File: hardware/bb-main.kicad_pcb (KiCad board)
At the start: 2 copper layers, 1 part, among them U2 BU33TD3WG-TR

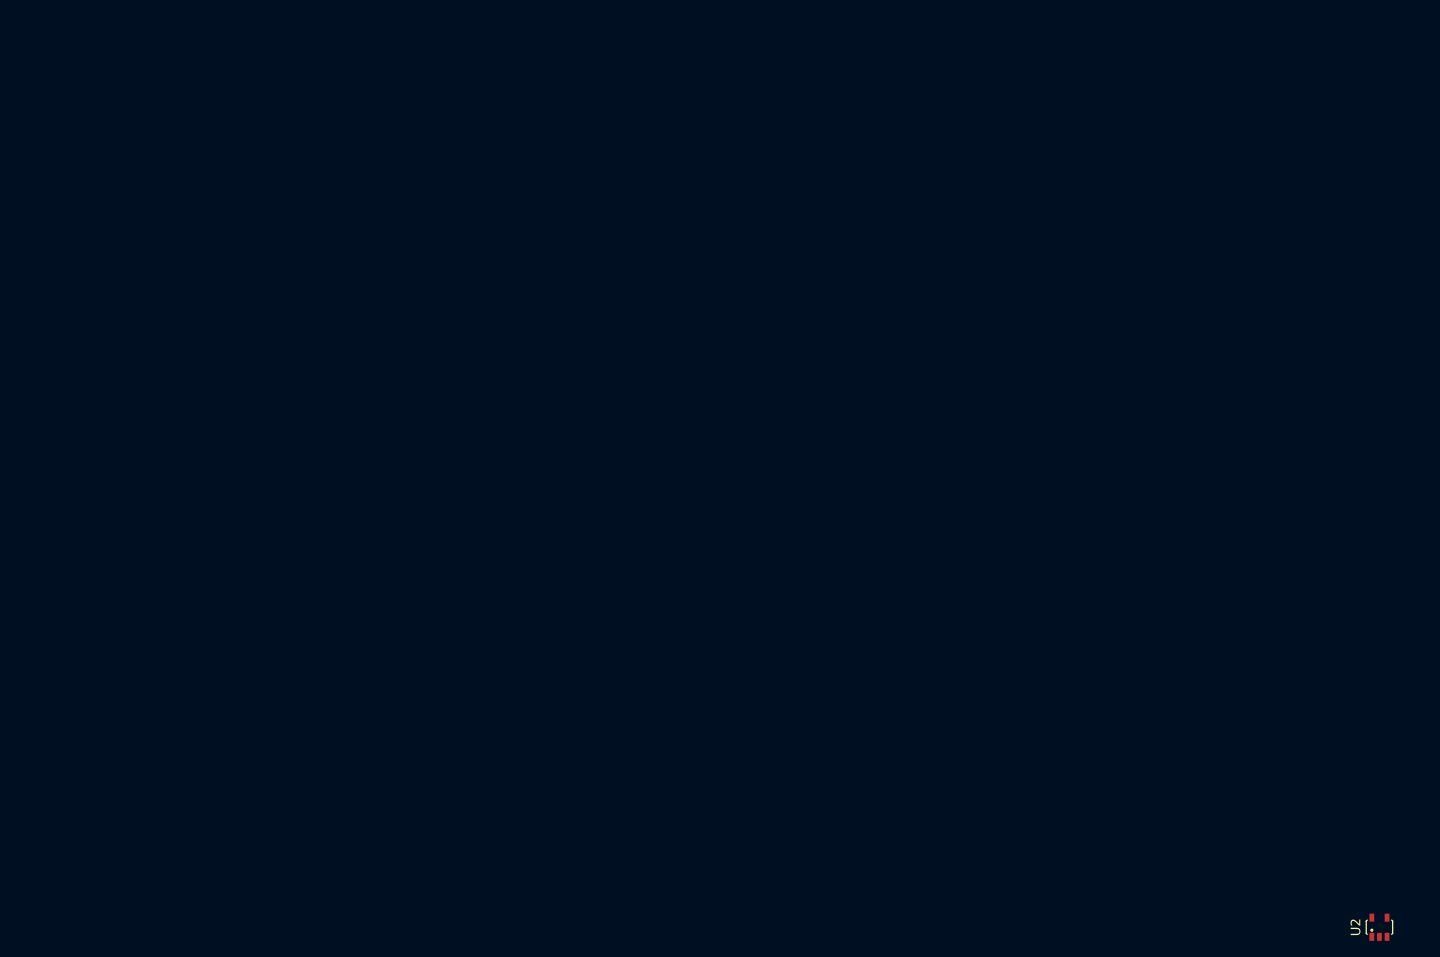
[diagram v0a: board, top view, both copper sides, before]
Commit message: Draw schematic components
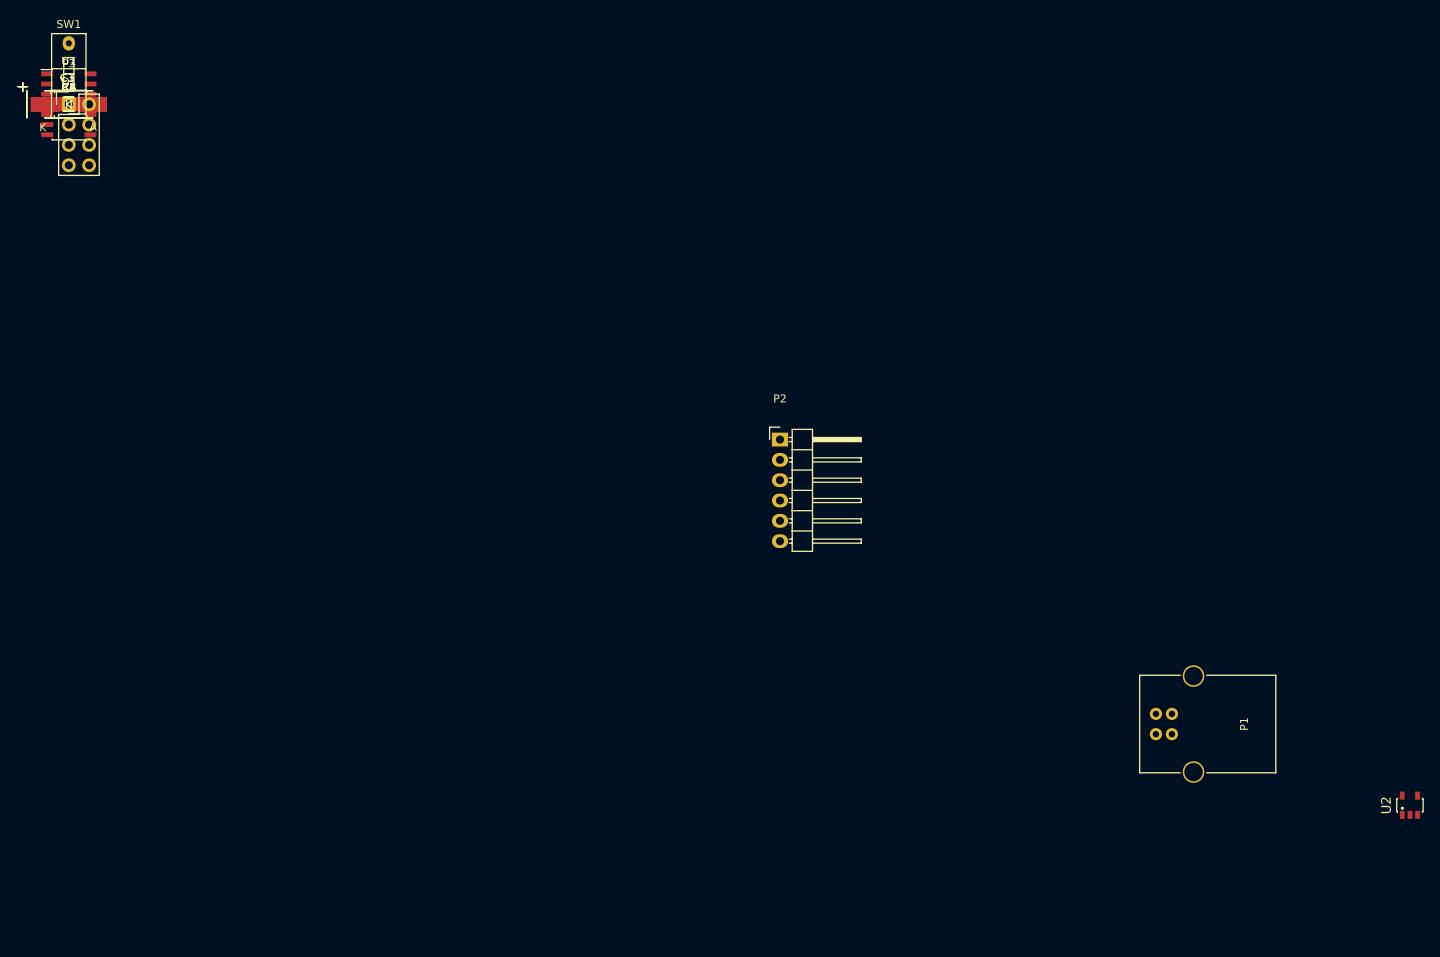
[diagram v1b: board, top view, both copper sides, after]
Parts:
- added C1: 10nF, Capacitors_Tantalum_SMD:TantalC_SizeC_EIA-6032_HandSoldering, F.Cu at (0.00, 0.00)
- added C2, C4: 100nF, Capacitors_SMD:C_0805_HandSoldering, F.Cu at (0.00, 0.00)
- added C3: 4.7uF, Capacitors_Tantalum_SMD:TantalC_SizeC_EIA-6032_HandSoldering, F.Cu at (0.00, 0.00)
- added C5, C6, C7: C, Capacitors_SMD:C_0805_HandSoldering, F.Cu at (0.00, 0.00)
- added D1: Led_Small, Diodes_SMD:SMA_Handsoldering, F.Cu at (0.00, 0.00)
- added P1: USB_B, Connect:USB_B, F.Cu at (135.9, 76.2)
- added P2: PICkit3, Pin_Headers:Pin_Header_Angled_1x06, F.Cu at (88.9, 41.9)
- added P3: OLED, Pin_Headers:Pin_Header_Straight_2x04, F.Cu at (0.00, 0.00)
- added R1: 10k, Resistors_SMD:R_0805_HandSoldering, F.Cu at (0.00, 0.00)
- added R2, R3, R4, R5: 4.7k, Resistors_SMD:R_0805_HandSoldering, F.Cu at (0.00, 0.00)
- added R6: 130, Resistors_SMD:R_0805_HandSoldering, F.Cu at (0.00, 0.00)
- added SW1: SW_PUSH, Buttons_Switches_ThroughHole:SW_DIP_x1_Slide, F.Cu at (0.00, 0.00)
- added U1: PIC16(L)F1455-I/SL, Housings_SOIC:SOIC-14_3.9x8.7mm_Pitch1.27mm, F.Cu at (0.00, 0.00)
- moved U2 15.7 mm to (167.6, 87.6)
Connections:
- U2 pad 1: Net-(U2-Pad1) -> +5V
- U2 pad 2: Net-(U2-Pad2) -> GND
- U2 pad 3: Net-(U2-Pad3) -> +5V
- U2 pad 5: Net-(U2-Pad5) -> +3V3

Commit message: Place components on the board
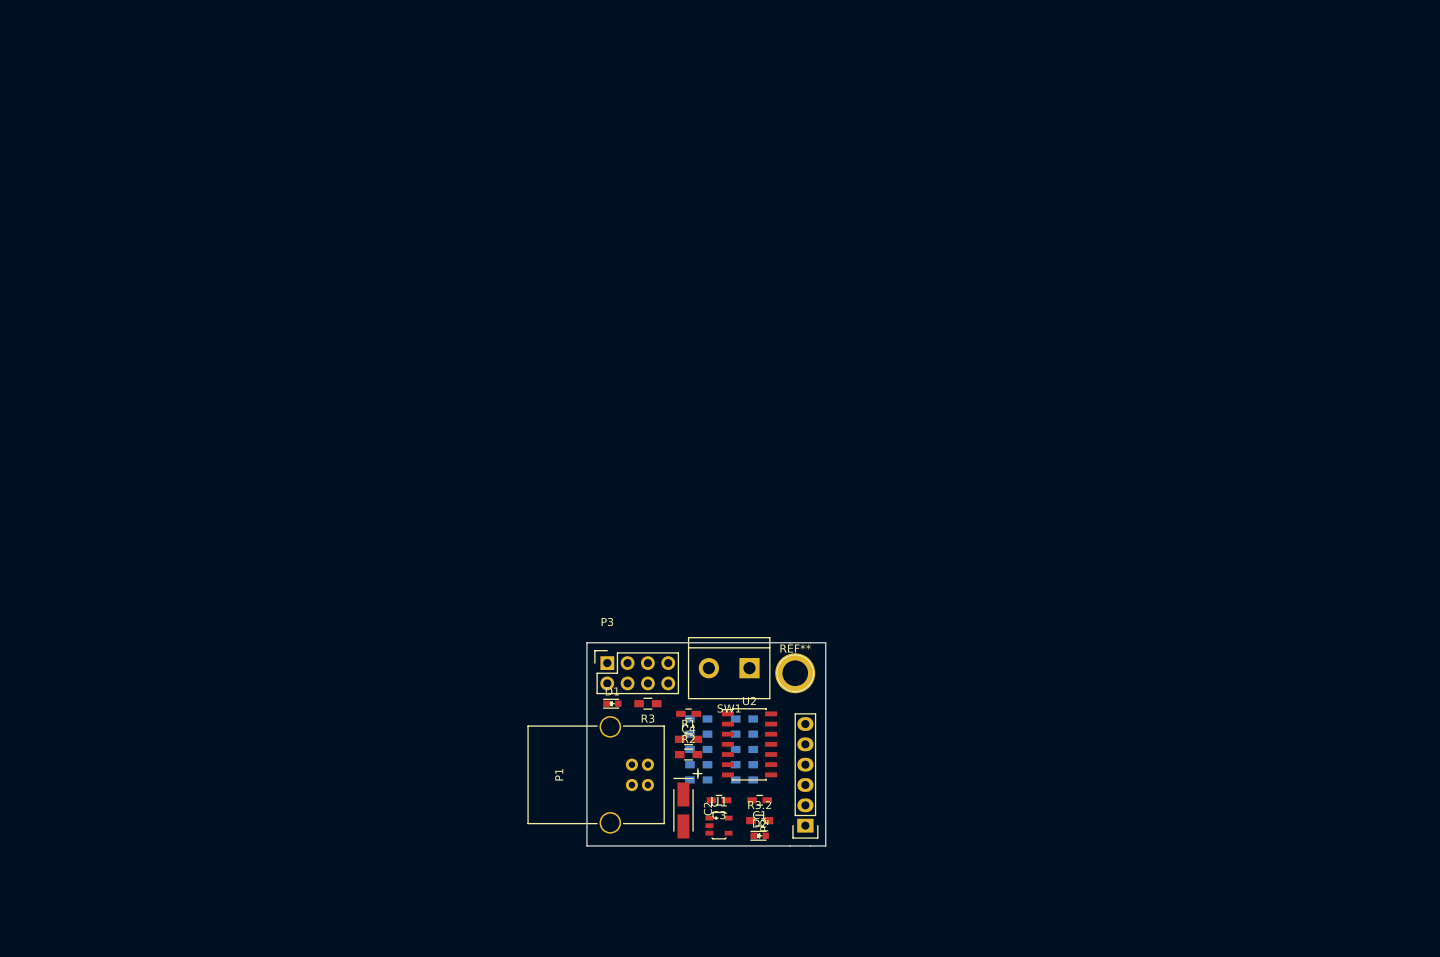
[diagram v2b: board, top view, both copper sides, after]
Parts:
- removed C5, C6, C7: C, Capacitors_SMD:C_0805_HandSoldering
- added D2: Led_Small, LEDs:LED_0603, F.Cu at (86.4, 91.4)
- added R10: 16k, Resistors_SMD:R_0603_HandSoldering, B.Cu at (78.7, 80.6)
- added R11: 16k, Resistors_SMD:R_0603_HandSoldering, B.Cu at (78.7, 82.5)
- added R12: 16k, Resistors_SMD:R_0603_HandSoldering, B.Cu at (78.7, 84.5)
- added R13: 16k, Resistors_SMD:R_0603_HandSoldering, B.Cu at (78.7, 76.8)
- added R3.2: 390, Resistors_SMD:R_0603_HandSoldering, F.Cu at (86.4, 89.5)
- added R7: 8.2k, Resistors_SMD:R_0603_HandSoldering, B.Cu at (84.5, 80.6)
- added R8: 8.2k, Resistors_SMD:R_0603_HandSoldering, B.Cu at (84.5, 78.7)
- added R9: 16k, Resistors_SMD:R_0603_HandSoldering, B.Cu at (78.7, 78.7)
- added REF**: 1pin, Connect:1pin, F.Cu at (90.8, 71.1)
- C1: value 10nF -> 470nF; footprint Capacitors_Tantalum_SMD:TantalC_SizeC_EIA-6032_HandSoldering -> Capacitors_SMD:C_0603_HandSoldering
- C2: value 100nF -> 10uF; footprint Capacitors_SMD:C_0805_HandSoldering -> Capacitors_Tantalum_SMD:TantalC_SizeA_EIA-3216_HandSoldering
- C3: value 4.7uF -> 100nF; footprint Capacitors_Tantalum_SMD:TantalC_SizeC_EIA-6032_HandSoldering -> Capacitors_SMD:C_0603_HandSoldering
- C4: footprint Capacitors_SMD:C_0805_HandSoldering -> Capacitors_SMD:C_0603_HandSoldering
- D1: footprint Diodes_SMD:SMA_Handsoldering -> LEDs:LED_0603
- P2: footprint Pin_Headers:Pin_Header_Angled_1x06 -> Socket_Strips:Socket_Strip_Straight_1x06
- P3: footprint Pin_Headers:Pin_Header_Straight_2x04 -> Socket_Strips:Socket_Strip_Straight_2x04
- R1: footprint Resistors_SMD:R_0805_HandSoldering -> Resistors_SMD:R_0603_HandSoldering
- R2: value 4.7k -> 10k; footprint Resistors_SMD:R_0805_HandSoldering -> Resistors_SMD:R_0603_HandSoldering
- R3: value 4.7k -> 390; footprint Resistors_SMD:R_0805_HandSoldering -> Resistors_SMD:R_0603_HandSoldering
- R4, R5: value 4.7k -> 8.2k; footprint Resistors_SMD:R_0805_HandSoldering -> Resistors_SMD:R_0603_HandSoldering; moved to B.Cu
- R6: value 130 -> 8.2k; footprint Resistors_SMD:R_0805_HandSoldering -> Resistors_SMD:R_0603_HandSoldering; moved to B.Cu
- SW1: footprint Buttons_Switches_ThroughHole:SW_DIP_x1_Slide -> Connect:bornier2
- U1: value PIC16(L)F1455-I/SL -> BU33TD3WG-TR; footprint Housings_SOIC:SOIC-14_3.9x8.7mm_Pitch1.27mm -> Housings_Proj:SSOP5
- U2: value BU33TD3WG-TR -> PIC16(L)F1455-I/SL; footprint SSOP5 -> Housings_SOIC:SOIC-14_3.9x8.7mm_Pitch1.27mm
- moved C1 122.6 mm to (86.4, 87.0), turned to 180 degrees
- moved U1 121.4 mm to (81.3, 90.2), turned to 270 degrees
- moved R5 119.4 mm to (84.5, 84.5), turned to 180 degrees
- moved C3 119.1 mm to (81.3, 87.0), turned to 180 degrees
- moved R6 118.1 mm to (84.5, 82.5), turned to 180 degrees
- moved C2 117.0 mm to (76.8, 88.3), turned to 270 degrees
- moved R4 114.2 mm to (84.5, 76.8), turned to 180 degrees
- moved R2 112.3 mm to (77.5, 81.3)
- moved R1 110.9 mm to (77.5, 79.4)
- moved C4 108.7 mm to (77.5, 76.2), turned to 180 degrees
- moved SW1 108.5 mm to (82.5, 70.5), turned to 180 degrees
- moved R3 104.2 mm to (72.4, 74.9), turned to 180 degrees
- moved D1 101.1 mm to (67.9, 74.9)
- moved P3 97.0 mm to (67.3, 69.8)
- moved U2 82.9 mm to (85.1, 80.0)
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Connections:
- C1 pad 1: +5V -> GND
- C1 pad 2: GND -> Net-(C1-Pad2)
- C2 pad 1: +3V3 -> +5V
- C4 pad 1: GND -> +5V
- C4 pad 2: Net-(C4-Pad2) -> GND
- P2 pad 2: +3V3 -> +5V
- P2 pad 4: /SDA -> /ICSPDAT/OLED_SCK
- P2 pad 5: /SCL -> /ICSPCLK
- P2 pad 6: Net-(P2-Pad6) -> (no net)
- P3 pad 2: /SDA -> /SDO
- P3 pad 3: /SCL -> /SCK
- P3 pad 4: /~RES~ -> /D/~C~
- P3 pad 7: Net-(P3-Pad7) -> /~RES~
- R1 pad 1: +3V3 -> +5V
- R2 pad 1: +3V3 -> +5V
- R2 pad 2: /SCL -> /BUT_1
- R3 pad 1: +3V3 -> /LED_A
- R3 pad 2: /SDA -> Net-(D1-Pad2)
- R4 pad 1: +3V3 -> /OLED_SDO
- R4 pad 2: /~RES~ -> /SDO
- R5 pad 1: +3V3 -> /ICSPDAT/OLED_SCK
- R5 pad 2: Net-(C7-Pad1) -> /SCK
- R6 pad 1: Net-(R6-Pad1) -> /OLED_D/~C~
- R6 pad 2: Net-(D1-Pad2) -> /D/~C~
- SW1 pad 1: Net-(C7-Pad1) -> /BUT_1
- U1 pad 1: +3V3 -> +5V
- U1 pad 2: Net-(U1-Pad2) -> GND
- U1 pad 3: Net-(U1-Pad3) -> +5V
- U1 pad 4: /~MCLR~ -> (no net)
- U1 pad 5: Net-(R6-Pad1) -> +3V3
- U2 pad 2: GND -> /LED_A
- U2 pad 3: +5V -> /BUT_1
- U2 pad 4: Net-(U2-Pad4) -> /~MCLR~
- U2 pad 5: +3V3 -> /OLED_~RES~
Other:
- board outline added: 29.8 x 25.4 mm
- net class Default: trace_width 0.25 -> 0.254
- rule pad_to_mask_clearance: 0.2 -> 0
- rule trace_min: 0.2 -> 0.1524
- rule via_min_drill: 0.3 -> 0.3302

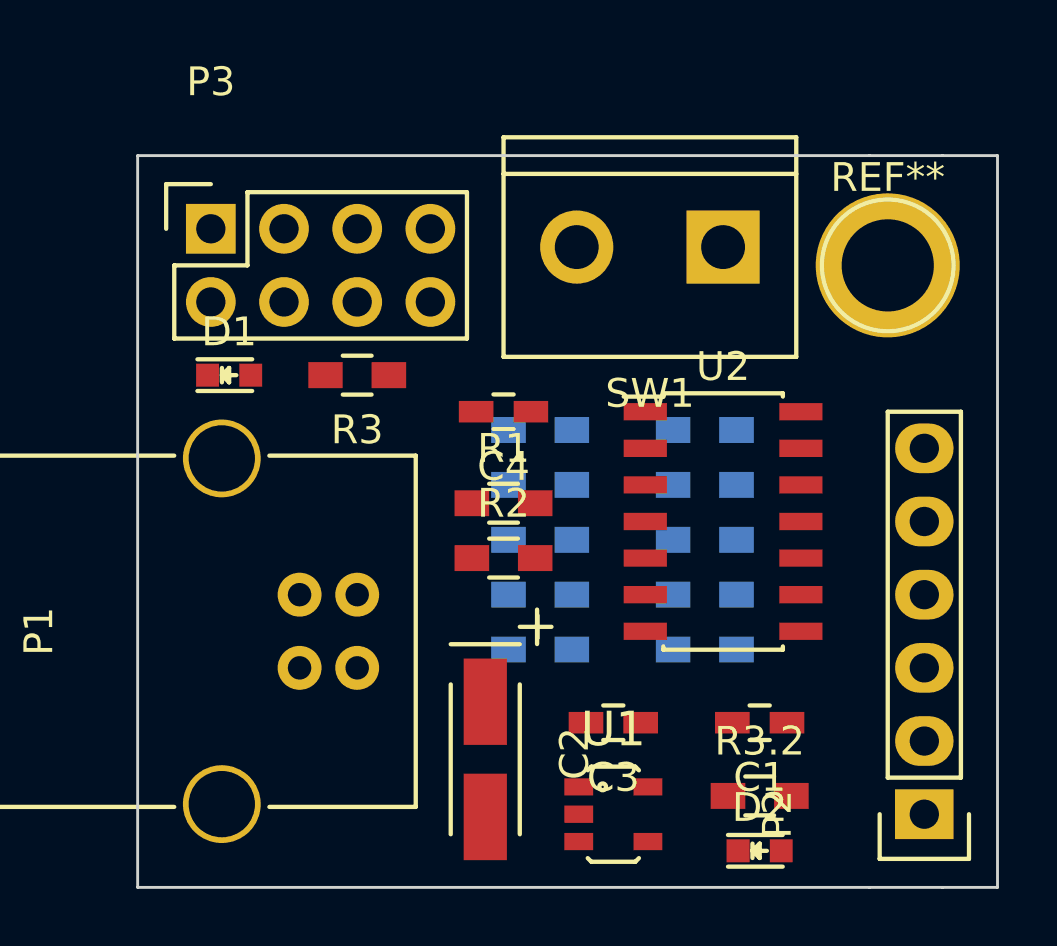
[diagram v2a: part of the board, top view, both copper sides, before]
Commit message: Add power new class
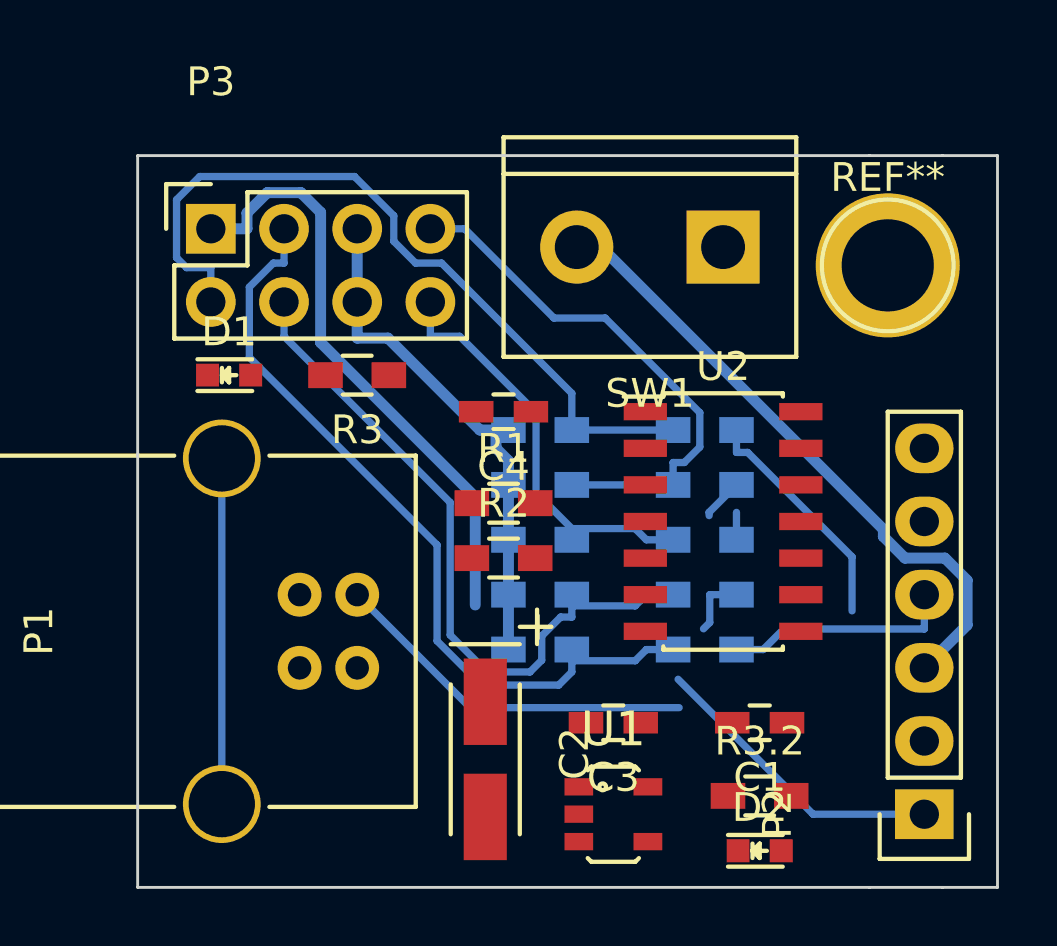
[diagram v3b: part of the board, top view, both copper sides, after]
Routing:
- net GND: track 0.00 -> 40.3 mm
- net /SCK: track 0.00 -> 27.7 mm
- net /SDO: track 0.00 -> 27.0 mm
- net /D/~C~: track 0.00 -> 24.4 mm
- net +3V3: track 0.00 -> 20.8 mm
- net /~RES~: track 0.00 -> 18.6 mm
- net /~CS~: track 0.00 -> 14.6 mm
- net Net-(P1-Pad2): track 0.00 -> 12.8 mm
- net Net-(P1-Pad5): track 0.00 -> 12.0 mm
- net /~MCLR~: track 0.00 -> 10.5 mm
- net /OLED_SDO: track 0.00 -> 8.17 mm
- net /ICSPDAT/OLED_SCK: track 0.00 -> 8.01 mm
- net /OLED_D/~C~: track 0.00 -> 2.20 mm
- net /OLED_~RES~: track 0.00 -> 1.46 mm
- net /OLED_~CS~: track 0.00 -> 0.95 mm
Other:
- net class Power added: clearance 0.2, trace_width 0.381, via_dia 0.6, via_drill 0.4

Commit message: Board changes
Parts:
- removed REF**: 1pin, Connect:1pin
- added MH1: , Mounting_Holes:MountingHole_4mm, F.Cu at (86.0, 76.0)
- D2: value Led_Small -> L1
- P1: footprint Connect:USB_B -> Connect:USB_Mini-B
- R10, R11, R12, R13, R4, R5, R6, R7, R8, R9: moved to F.Cu
- moved P3 36.3 mm to (103.6, 71.1), turned to 270 degrees
- moved R12 33.0 mm to (109.7, 73.2), turned to 180 degrees
- moved R11 31.9 mm to (109.7, 75.2), turned to 180 degrees
- moved R13 31.5 mm to (109.7, 71.1), turned to 180 degrees
- moved R10 31.2 mm to (109.7, 77.2), turned to 180 degrees
- moved R9 31.0 mm to (109.7, 79.2), turned to 180 degrees
- moved U1 26.4 mm to (60.5, 73.9)
- moved R3.2 25.8 mm to (65.5, 74.3), turned to 270 degrees
- moved SW1 25.7 mm to (97.8, 91.2), turned to 0 degrees
- moved D2 24.4 mm to (65.5, 78.7), turned to 90 degrees
- moved C1 21.9 mm to (67.6, 75.8), turned to 270 degrees
- moved C3 21.7 mm to (63.8, 74.2), turned to 270 degrees
- moved C2 21.2 mm to (65.0, 70.6), turned to 0 degrees
- moved D1 19.4 mm to (77.7, 91.7)
- moved R3 16.6 mm to (80.0, 89.7), turned to 0 degrees
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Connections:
- P2 pad 6: (no net) -> Net-(P2-Pad6)
- U1 pad 4: (no net) -> Net-(U1-Pad4)
- U2 pad 2: /LED_A -> /BUT_1
- U2 pad 3: /BUT_1 -> /LED_A
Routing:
- net +3V3: track 20.8 -> 0.39 mm
- net GND: track 40.3 -> 21.9 mm, vias 0 -> 2
- net /SCK: track 27.7 -> 13.5 mm
- net /SDO: track 27.0 -> 13.5 mm
- net Net-(P1-Pad5): track 12.0 -> 0.00 mm
- net /D/~C~: track 24.4 -> 13.8 mm
- net /~MCLR~: track 10.5 -> 1.92 mm
- net /OLED_SDO: track 8.17 -> 0.15 mm
- net Net-(P1-Pad3): track 0.00 -> 7.57 mm
- net /ICSPDAT/OLED_SCK: track 8.01 -> 0.45 mm
- net Net-(P1-Pad2): track 12.8 -> 7.76 mm
- net /~RES~: track 18.6 -> 13.7 mm
- net Net-(D2-Pad2): track 0.00 -> 2.54 mm
- net /OLED_D/~C~: track 2.20 -> 0.15 mm
- net /OLED_~RES~: track 1.46 -> 0.00 mm
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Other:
- board size 29.8 x 25.4 mm -> 62 x 19 mm
